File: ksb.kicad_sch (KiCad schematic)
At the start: 23 parts, among them J8 Conn_01x02, U15 74LVC1G14

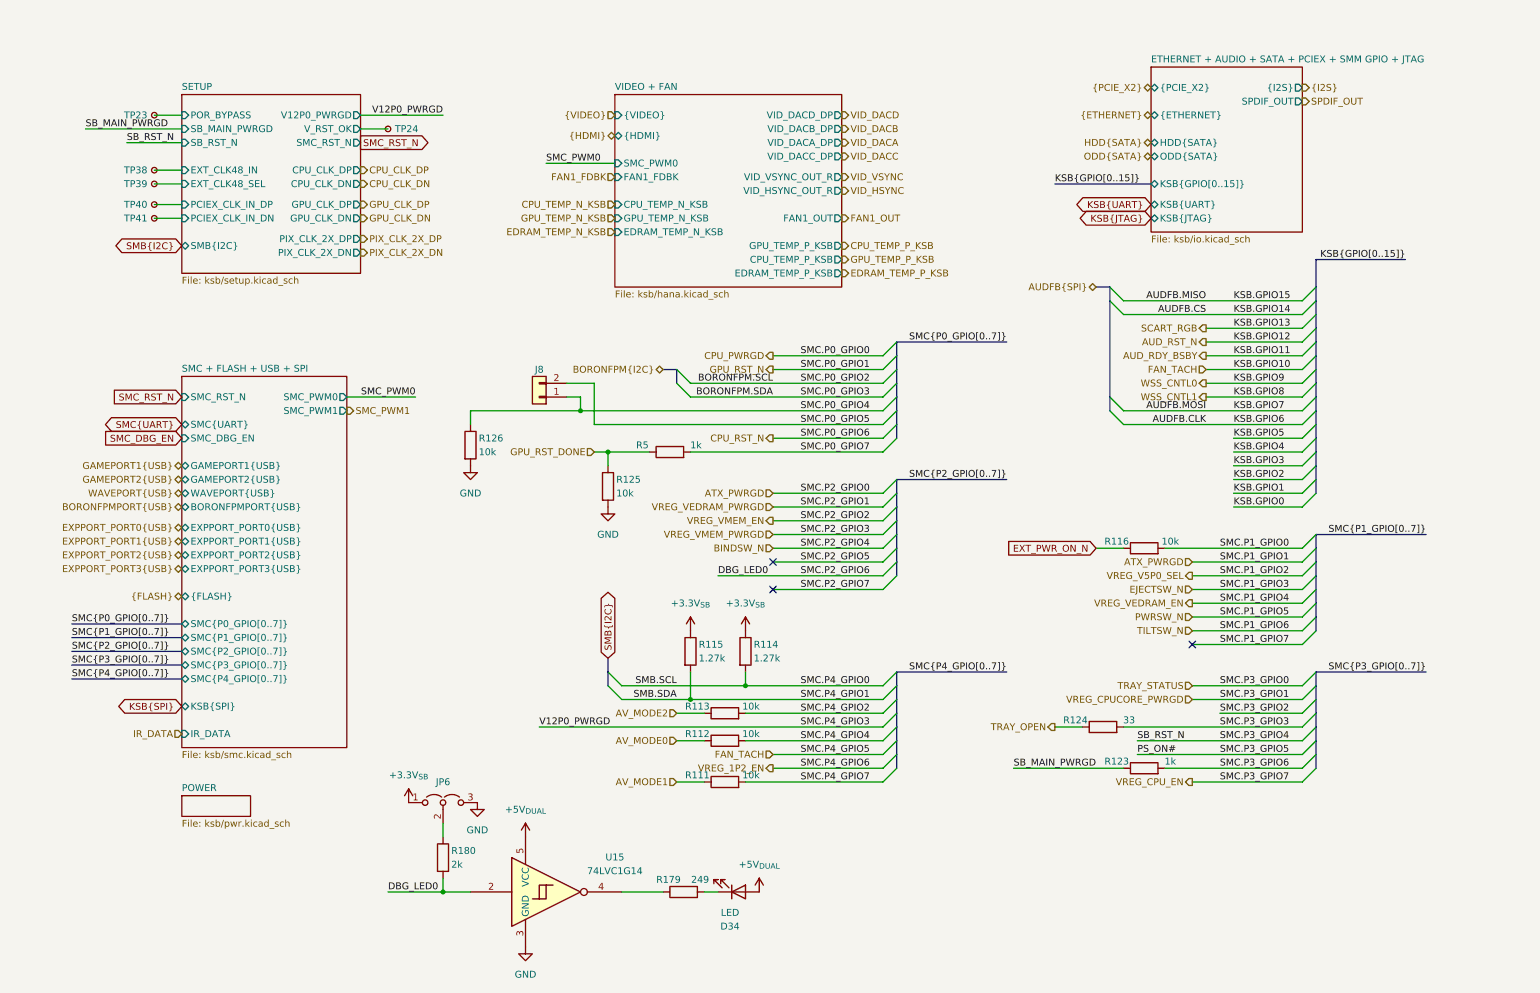
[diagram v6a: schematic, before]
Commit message: Multipurpose and standby power rails, Reannotated schematic
Added V_1P2, V_1P8, V_5P0DUAL, V_EFUSE, V_GPUPCIE, V_3P3STBY and V_1P2STBY
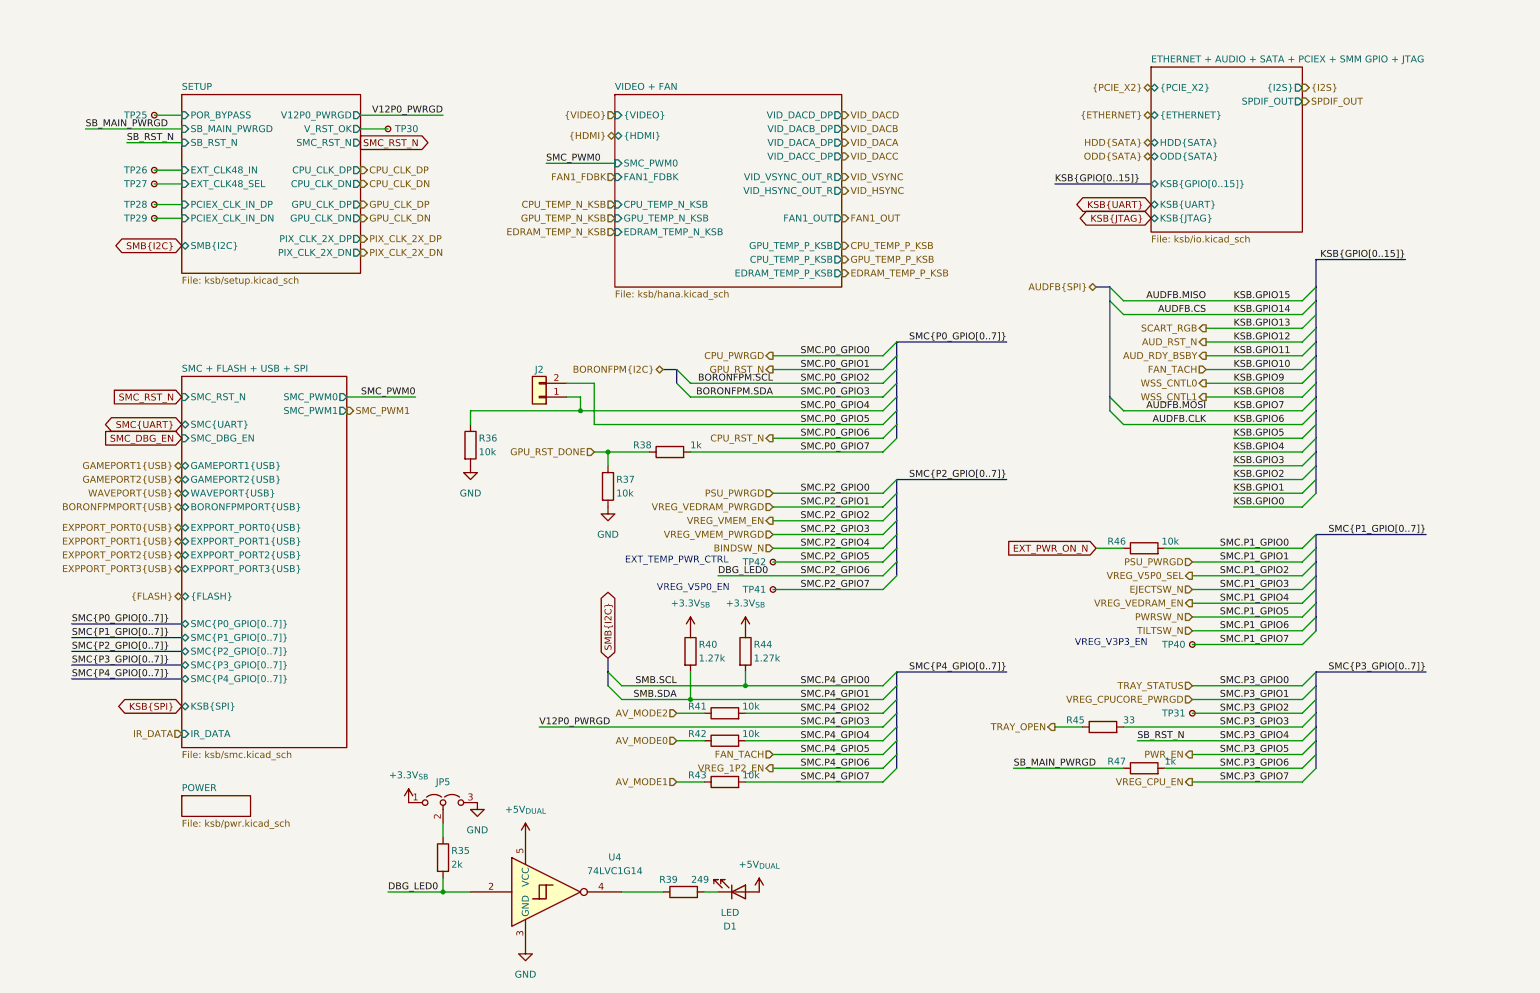
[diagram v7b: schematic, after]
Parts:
- added TP31, TP40, TP41, TP42: TestPoint_Small, symbol Connector:TestPoint_Small
- renumbered D34 to D1, J8 to J2, JP6 to JP5, R180 to R35, R126 to R36, R125 to R37, R5 to R38, R179 to R39, R115 to R40, R113 to R41, R112 to R42, R111 to R43, R114 to R44, R124 to R45, R116 to R46, R123 to R47, TP23 to TP25, TP38 to TP26, TP39 to TP27, TP40 to TP28, TP41 to TP29, TP24 to TP30, U15 to U4
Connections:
- net SMC.P1_GPIO7: now also TP40.1
- net SMC.P2_GPIO5: now also TP42.1
- net SMC.P2_GPIO7: now also TP41.1
- net SMC.P3_GPIO2: now also TP31.1
- no-connect marks 3 -> 0
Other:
- note added: "EXT_TEMP_PWR_CTRL"
- note added: "VREG_V3P3_EN"
- note added: "VREG_V5P0_EN"
